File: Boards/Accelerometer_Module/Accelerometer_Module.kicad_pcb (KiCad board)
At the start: 2 copper layers, 66.2 x 66.2 mm, 55 parts, among them J1 CONN_02X03, J2 SD_socket, SW1 SW_Push_SPST_NO, U1 ATmega328P-AU, U101 TPS560430YF, U2 LIS3DHTR, U3 INA260

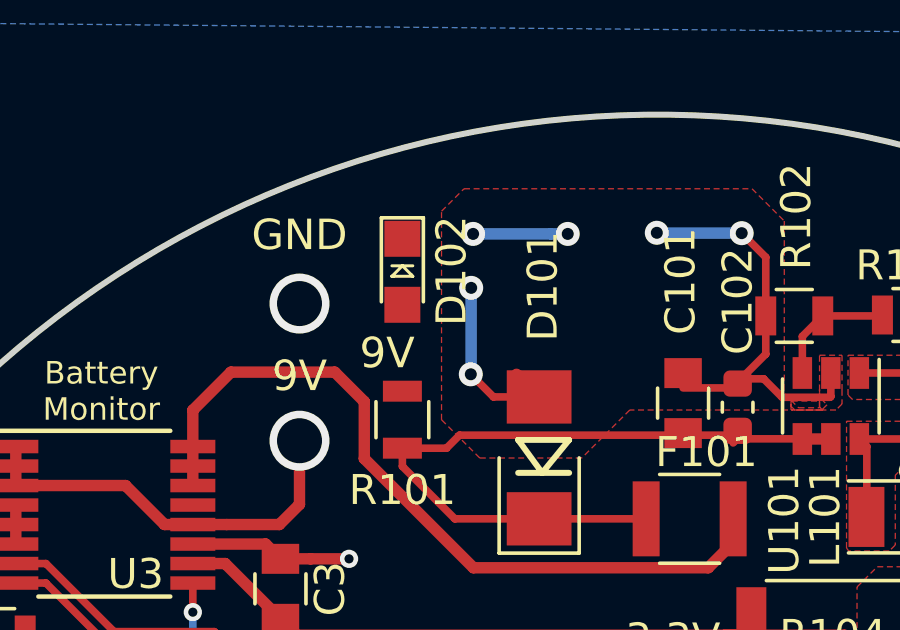
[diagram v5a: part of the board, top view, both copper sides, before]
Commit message: Adding 9V LED Trace
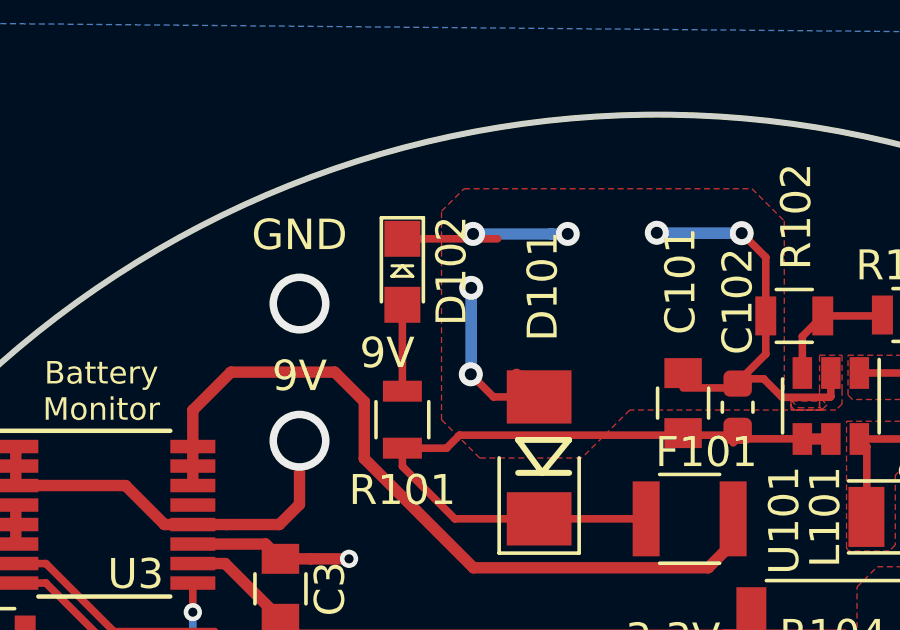
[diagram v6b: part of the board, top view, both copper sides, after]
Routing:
- net GND: track 106.3 -> 109.5 mm
- net Net-(D102-Pad2): track 0.00 -> 2.88 mm
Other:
- rule via_min_size: 0.1524 -> 0.6096
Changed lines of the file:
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@@
     (thickness 1.6)
     (drawings 26)
-    (tracks 583)
+    (tracks 585)
     (zones 0)
     (modules 55)
@@
   )
   (setup
-    (last_trace_width 0.381)
+    (last_trace_width 0.254)
     (user_trace_width 0.254)
     (user_trace_width 0.381)
@@
     (via_size 0.6096)
     (via_drill 0.3048)
-    (via_min_size 0.1524)
+    (via_min_size 0.6096)
     (via_min_drill 0.3048)
     (user_via 0.6096 0.3048)
@@
   (segment (start 60.071 99.568) (end 59.578 99.075) (width 0.381) (layer F.Cu) (net 1))
   (segment (start 51.25 97.775) (end 51.25 99.075) (width 0.381) (layer F.Cu) (net 1))
-  (segment (start 57.15 95.825) (end 57.15 97.125) (width 0.381) (layer F.Cu) (net 53))
   (segment (start 53.213 115.57) (end 53.213 119.253) (width 0.381) (layer B.Cu) (net 1))
   (segment (start 78.916 115.951) (end 77.316 114.351) (width 0.254) (layer F.Cu) (net 1))
@@
   (segment (start 89.068 136.439) (end 89.068 136.439) (width 0.381) (layer F.Cu) (net 1))
   (via (at 89.068 136.439) (size 0.6096) (drill 0.3048) (layers F.Cu B.Cu) (net 1))
+  (segment (start 64.135 88.9) (end 67.31 88.9) (width 0.254) (layer F.Cu) (net 1))
   (segment (start 77.44 103.03088) (end 77.44 104.303) (width 0.254) (layer F.Cu) (net 2))
   (segment (start 76.5222 102.11308) (end 77.44 103.03088) (width 0.254) (layer F.Cu) (net 2))
@@
   (segment (start 65.60568 95.88) (end 64.135 95.88) (width 0.254) (layer F.Cu) (net 3))
   (segment (start 66.04 95.44568) (end 65.60568 95.88) (width 0.254) (layer F.Cu) (net 3))
+  (segment (start 68.64666 98.28214) (end 68.6943 98.2345) (width 0.381) (layer F.Cu) (net 3))
+  (segment (start 68.6943 98.2345) (end 68.52666 98.40214) (width 0.381) (layer F.Cu) (net 3))
+  (segment (start 72.2608 98.2345) (end 68.6943 98.2345) (width 0.254) (layer F.Cu) (net 3))
+  (segment (start 67.3608 98.2345) (end 68.6943 98.2345) (width 0.254) (layer F.Cu) (net 3))
+  (segment (start 65.8855 98.2345) (end 67.3608 98.2345) (width 0.254) (layer F.Cu) (net 3))
+  (segment (start 64.135 96.484) (end 65.8855 98.2345) (width 0.254) (layer F.Cu) (net 3))
+  (segment (start 64.135 95.88) (end 64.135 96.484) (width 0.254) (layer F.Cu) (net 3))
   (segment (start 79.3676 97.92444) (end 79.6167 98.17354) (width 0.25) (layer F.Cu) (net 4))
   (segment (start 81.627 95.5728) (end 81.7118 95.488) (width 0.254) (layer F.Cu) (net 4))
@@
   (segment (start 84.1883 93.0356) (end 82.63842 91.48572) (width 0.254) (layer F.Cu) (net 6))
   (segment (start 84.1883 95.758) (end 84.1883 93.0356) (width 0.254) (layer F.Cu) (net 6))
+  (segment (start 64.135 93.98) (end 64.135 91.1) (width 0.254) (layer F.Cu) (net 7))
   (segment (start 77.44 106.807) (end 77.44 108.557) (width 0.254) (layer F.Cu) (net 8))
   (segment (start 80.11918 91.47048) (end 80.13442 91.48572) (width 0.254) (layer F.Cu) (net 9))
@@
   (segment (start 83.185 131.0705) (end 83.185 138.557) (width 0.254) (layer F.Cu) (net 16))
   (segment (start 91.946897 122.308603) (end 83.185 131.0705) (width 0.254) (layer F.Cu) (net 16))
-  (via (at 60.706 95.631) (size 2) (drill 1.5) (layers F.Cu B.Cu) (net 54))
-  (segment (start 68.64666 98.28214) (end 68.6943 98.2345) (width 0.381) (layer F.Cu) (net 3))
-  (segment (start 68.6943 98.2345) (end 68.52666 98.40214) (width 0.381) (layer F.Cu) (net 3))
-  (segment (start 72.2608 98.2345) (end 68.6943 98.2345) (width 0.254) (layer F.Cu) (net 3))
-  (segment (start 67.3608 98.2345) (end 68.6943 98.2345) (width 0.254) (layer F.Cu) (net 3))
-  (segment (start 65.8855 98.2345) (end 67.3608 98.2345) (width 0.254) (layer F.Cu) (net 3))
-  (segment (start 64.135 96.484) (end 65.8855 98.2345) (width 0.254) (layer F.Cu) (net 3))
-  (segment (start 64.135 95.88) (end 64.135 96.484) (width 0.254) (layer F.Cu) (net 3))
-  (segment (start 51.25 95.825) (end 51.25 96.475) (width 0.381) (layer F.Cu) (net 54))
-  (segment (start 51.25 96.475) (end 51.25 97.125) (width 0.381) (layer F.Cu) (net 54))
-  (segment (start 56.207778 98.425) (end 57.15 98.425) (width 0.381) (layer F.Cu) (net 54))
-  (segment (start 54.907778 97.125) (end 56.207778 98.425) (width 0.381) (layer F.Cu) (net 54))
-  (segment (start 51.25 97.125) (end 54.907778 97.125) (width 0.381) (layer F.Cu) (net 54))
-  (segment (start 60.706 95.84732) (end 60.72886 95.87018) (width 0.381) (layer F.Cu) (net 54))
   (segment (start 79.121 114.056) (end 79.416 114.351) (width 0.254) (layer F.Cu) (net 17))
   (segment (start 79.121 112.649) (end 79.121 114.056) (width 0.254) (layer F.Cu) (net 17))
@@
   (segment (start 66.4845 138.443448) (end 64.439052 136.398) (width 0.254) (layer F.Cu) (net 52))
   (segment (start 66.4845 138.8745) (end 66.4845 138.443448) (width 0.254) (layer F.Cu) (net 52))
+  (segment (start 57.15 95.825) (end 57.15 97.125) (width 0.381) (layer F.Cu) (net 53))
   (segment (start 57.15 95.825) (end 57.15 94.615) (width 0.381) (layer F.Cu) (net 53))
   (segment (start 57.15 94.615) (end 58.42 93.345) (width 0.381) (layer F.Cu) (net 53))
@@
   (segment (start 62.865 96.227222) (end 66.503278 99.8655) (width 0.381) (layer F.Cu) (net 53))
   (segment (start 62.865 94.327222) (end 62.865 96.227222) (width 0.381) (layer F.Cu) (net 53))
+  (via (at 60.706 95.631) (size 2) (drill 1.5) (layers F.Cu B.Cu) (net 54))
+  (segment (start 51.25 95.825) (end 51.25 96.475) (width 0.381) (layer F.Cu) (net 54))
+  (segment (start 51.25 96.475) (end 51.25 97.125) (width 0.381) (layer F.Cu) (net 54))
+  (segment (start 56.207778 98.425) (end 57.15 98.425) (width 0.381) (layer F.Cu) (net 54))
+  (segment (start 54.907778 97.125) (end 56.207778 98.425) (width 0.381) (layer F.Cu) (net 54))
+  (segment (start 51.25 97.125) (end 54.907778 97.125) (width 0.381) (layer F.Cu) (net 54))
+  (segment (start 60.706 95.84732) (end 60.72886 95.87018) (width 0.381) (layer F.Cu) (net 54))
   (segment (start 60.03332 98.425) (end 58.281 98.425) (width 0.381) (layer F.Cu) (net 54))
   (segment (start 60.706 97.75232) (end 60.03332 98.425) (width 0.381) (layer F.Cu) (net 54))
